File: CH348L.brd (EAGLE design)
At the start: 99.1 x 80 mm, 43 parts, among them U1 AMS1117-3.3, U5 ESDU5V0H4, Y1 NX5032GA-8MHZ

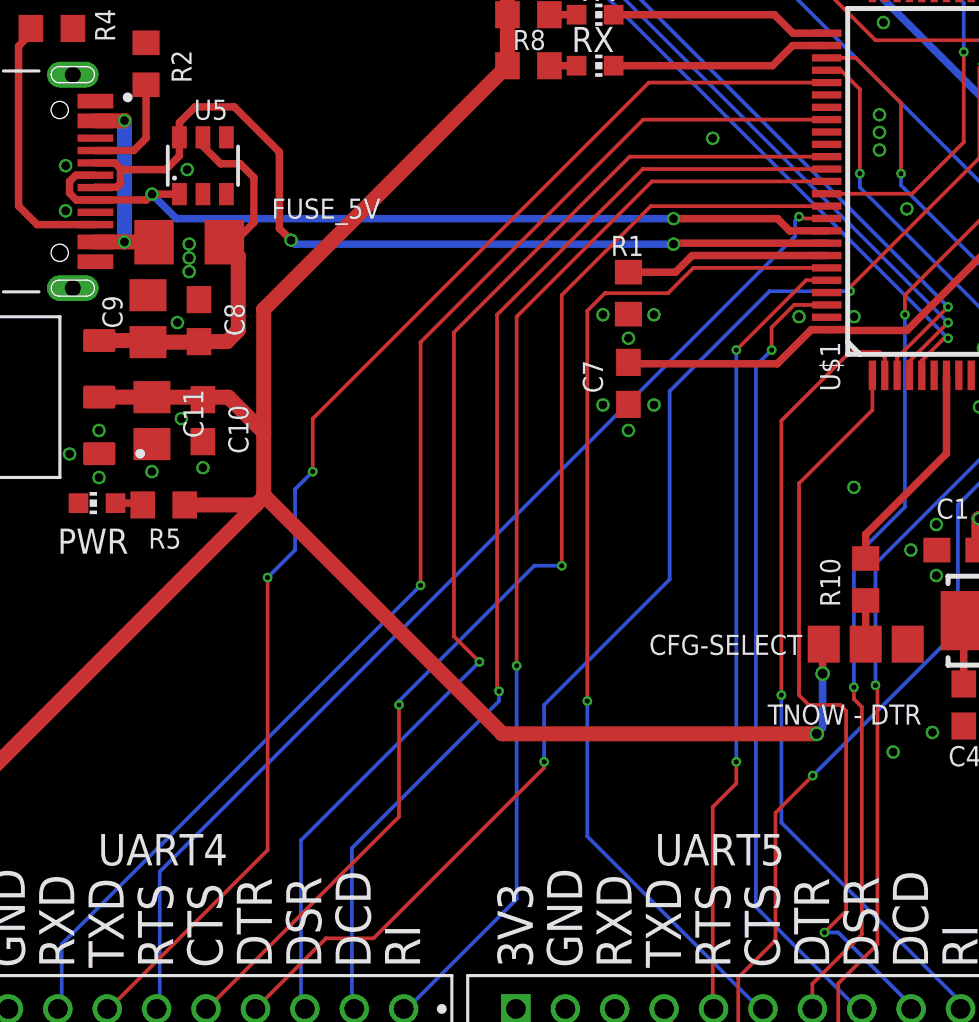
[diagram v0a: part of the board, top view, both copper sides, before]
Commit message: Fixed UD+ UD- swap
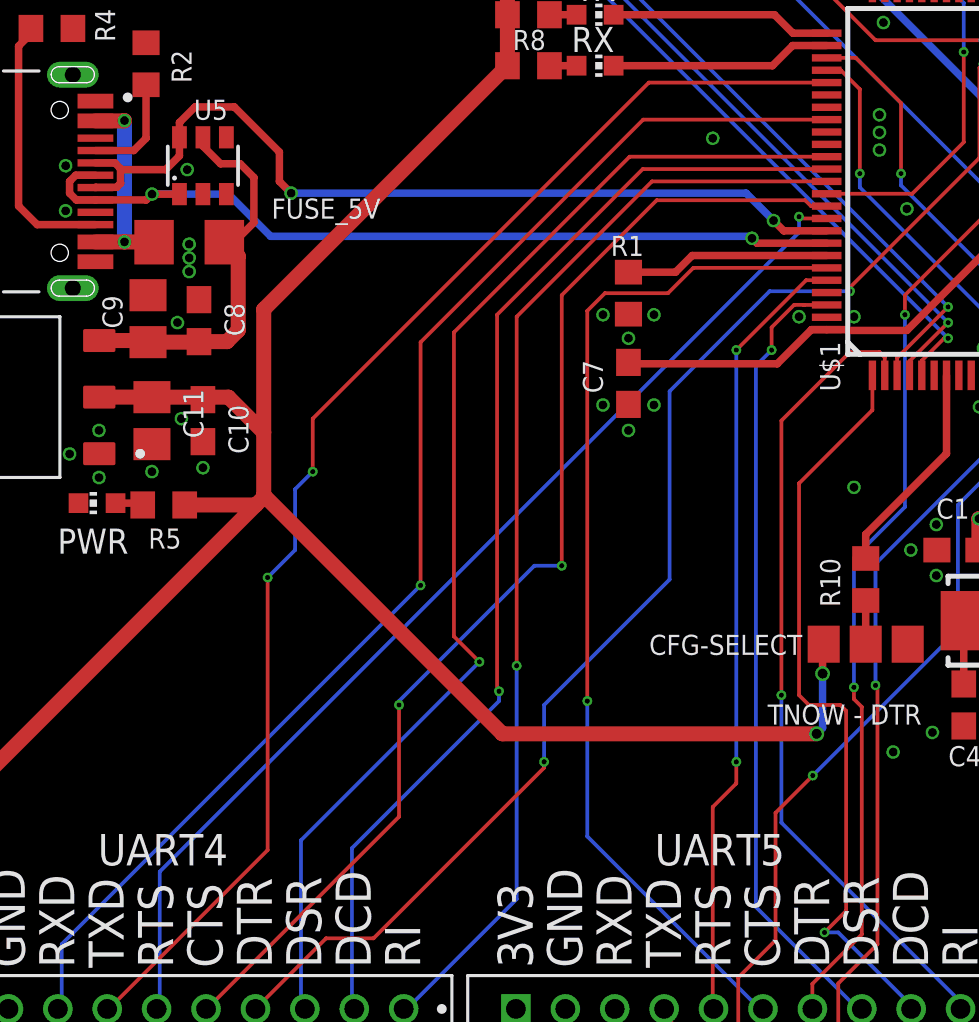
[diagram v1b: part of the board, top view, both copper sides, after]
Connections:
- net UD+: now also U$1.93; no longer U$1.92
- net UD-: now also U$1.92; no longer U$1.93
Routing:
- net UD-: track 37.4 -> 36.0 mm
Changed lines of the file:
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@@
 <setting verticaltext="up"/>
 </settings>
-<grid distance="25" unitdist="mil" unit="mil" style="lines" multiple="1" display="yes" altdistance="5" altunitdist="mil" altunit="mil"/>
+<grid distance="3.125" unitdist="mil" unit="mil" style="lines" multiple="1" display="yes" altdistance="5" altunitdist="mil" altunit="mil"/>
 <layers>
 <layer number="1" name="Top" color="4" fill="1" visible="yes" active="yes"/>
@@
 <contactref element="USBC" pad="B6"/>
 <contactref element="U5" pad="1"/>
-<contactref element="U$1" pad="92"/>
 <wire x1="14.064375" y1="39.255" x2="13.29125" y2="39.255" width="0.3048" layer="1"/>
 <wire x1="13.29125" y1="39.255" x2="13.0175" y2="39.52875" width="0.3048" layer="1"/>
@@
 <wire x1="16.35375" y1="39.49" x2="17.465" y2="39.49" width="0.3048" layer="1"/>
 <wire x1="16.35375" y1="39.49" x2="16.11875" y2="39.255" width="0.3048" layer="1"/>
-<wire x1="43.664375" y1="38.005" x2="42.16375" y2="38.005" width="0.3048" layer="1"/>
-<wire x1="42.16375" y1="38.005" x2="41.671875" y2="38.496875" width="0.3048" layer="1"/>
-<wire x1="41.671875" y1="38.496875" x2="37.465" y2="38.496875" width="0.3048" layer="1"/>
-<via x="37.465" y="38.496875" extent="1-16" drill="0.35"/>
-<wire x1="37.465" y1="38.496875" x2="17.346875" y2="38.496875" width="0.3048" layer="16"/>
-<wire x1="17.346875" y1="38.496875" x2="16.35375" y2="39.49" width="0.3048" layer="16"/>
+<via x="40.64" y="37.703125" extent="1-16" drill="0.35"/>
+<wire x1="40.64" y1="37.703125" x2="40.560625" y2="37.7825" width="0.3048" layer="16"/>
+<wire x1="40.560625" y1="37.7825" x2="21.156875" y2="37.7825" width="0.3048" layer="16"/>
+<wire x1="21.156875" y1="37.7825" x2="19.449375" y2="39.49" width="0.3048" layer="16"/>
+<wire x1="19.449375" y1="39.49" x2="16.35375" y2="39.49" width="0.3048" layer="16"/>
 <via x="16.35375" y="39.49" extent="1-16" drill="0.35"/>
+<contactref element="U$1" pad="93"/>
+<wire x1="43.664375" y1="37.505" x2="40.838125" y2="37.505" width="0.3048" layer="1"/>
+<wire x1="40.838125" y1="37.505" x2="40.64" y2="37.703125" width="0.3048" layer="1"/>
 </signal>
 <signal name="UD-">
@@
 <contactref element="USBC" pad="B7"/>
 <contactref element="U5" pad="6"/>
-<contactref element="U$1" pad="93"/>
 <wire x1="14.064375" y1="39.755" x2="14.07625" y2="39.766875" width="0.3048" layer="1"/>
 <wire x1="14.07625" y1="39.766875" x2="14.9225" y2="39.766875" width="0.3048" layer="1"/>
@@
 <wire x1="16.906875" y1="40.48125" x2="15.08125" y2="40.48125" width="0.3048" layer="1"/>
 <wire x1="17.465" y1="41.039375" x2="16.906875" y2="40.48125" width="0.3048" layer="1"/>
-<wire x1="43.664375" y1="37.505" x2="37.505" y2="37.505" width="0.3048" layer="1"/>
-<wire x1="37.505" y1="37.505" x2="37.465" y2="37.465" width="0.3048" layer="1"/>
-<via x="37.465" y="37.465" extent="1-16" drill="0.35"/>
-<wire x1="37.465" y1="37.465" x2="22.145625" y2="37.465" width="0.3048" layer="16"/>
-<wire x1="22.145625" y1="37.465" x2="21.986875" y2="37.62375" width="0.3048" layer="16"/>
-<via x="21.986875" y="37.62375" extent="1-16" drill="0.35"/>
-<wire x1="21.510625" y1="41.195625" x2="21.510625" y2="38.1" width="0.3048" layer="1"/>
-<wire x1="21.986875" y1="37.62375" x2="21.510625" y2="38.1" width="0.3048" layer="1"/>
+<via x="41.513125" y="38.4175" extent="1-16" drill="0.35"/>
+<wire x1="41.513125" y1="38.4175" x2="40.401875" y2="39.52875" width="0.3048" layer="16"/>
+<wire x1="40.401875" y1="39.52875" x2="21.986875" y2="39.52875" width="0.3048" layer="16"/>
+<via x="21.986875" y="39.52875" extent="1-16" drill="0.35"/>
+<wire x1="21.510625" y1="41.195625" x2="21.510625" y2="40.005" width="0.3048" layer="1"/>
+<wire x1="21.986875" y1="39.52875" x2="21.510625" y2="40.005" width="0.3048" layer="1"/>
 <wire x1="21.510625" y1="41.195625" x2="19.685" y2="43.02125" width="0.3048" layer="1"/>
 <wire x1="17.465" y1="42.38875" x2="17.465" y2="41.79" width="0.3048" layer="1"/>
@@
 <wire x1="18.0975" y1="43.02125" x2="17.465" y2="42.38875" width="0.3048" layer="1"/>
 <wire x1="14.064375" y1="40.755" x2="14.84986875" y2="40.755" width="0.3048" layer="1"/>
+<contactref element="U$1" pad="92"/>
+<wire x1="43.664375" y1="38.005" x2="41.925625" y2="38.005" width="0.3048" layer="1"/>
+<wire x1="41.925625" y1="38.005" x2="41.513125" y2="38.4175" width="0.3048" layer="1"/>
 </signal>
 <signal name="+3V3">
@@
 <contactref element="U$1" pad="91"/>
 <contactref element="UART4" pad="5"/>
-<wire x1="42.545" y1="38.57625" x2="42.38625" y2="38.4175" width="0.1524" layer="16"/>
-<wire x1="42.38625" y1="38.4175" x2="42.38625" y2="37.7825" width="0.1524" layer="16"/>
-<wire x1="16.66875" y1="12.065" x2="42.38625" y2="37.7825" width="0.1524" layer="16"/>
+<wire x1="42.545" y1="38.57625" x2="42.545" y2="37.94125" width="0.1524" layer="16"/>
+<wire x1="16.66875" y1="12.065" x2="42.545" y2="37.94125" width="0.1524" layer="16"/>
 <wire x1="16.66875" y1="6.50875" x2="16.66875" y2="12.065" width="0.1524" layer="16"/>
 <wire x1="16.66875" y1="6.50875" x2="16.541875" y2="6.50875" width="0.1524" layer="16"/>
@@
 <contactref element="U$1" pad="90"/>
 <contactref element="UART4" pad="6"/>
-<wire x1="32.940625" y1="35.40125" x2="36.544375" y2="39.005" width="0.1524" layer="1"/>
+<wire x1="32.940625" y1="35.40125" x2="36.7825" y2="39.243125" width="0.1524" layer="1"/>
 <wire x1="32.940625" y1="24.4475" x2="32.940625" y2="35.40125" width="0.1524" layer="1"/>
 <wire x1="26.3525" y1="18.811875" x2="26.3525" y2="18.970625" width="0.1524" layer="16"/>
@@
 <via x="32.940625" y="24.4475" extent="1-16" drill="0.2"/>
 <via x="26.3525" y="18.811875" extent="1-16" drill="0.2"/>
-<wire x1="43.664375" y1="39.005" x2="36.544375" y2="39.005" width="0.1524" layer="1"/>
+<wire x1="43.664375" y1="39.005" x2="43.029375" y2="39.005" width="0.1524" layer="1"/>
+<wire x1="43.029375" y1="39.005" x2="42.79125" y2="39.243125" width="0.1524" layer="1"/>
+<wire x1="42.79125" y1="39.243125" x2="36.7825" y2="39.243125" width="0.1524" layer="1"/>
 </signal>
 <signal name="DTR4">
